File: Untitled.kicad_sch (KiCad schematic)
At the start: 49 parts, among them J1 USB_OTG, J2 Conn_02x03_Odd_Even, J3 Conn_02x08_Odd_Even, J4 CONN_01X14, J5 CONN_01X14, J6 USB_OTG, Q1 LM317AG-TN3-R, SW1 SW_Push, U1 ICE40LP8K-CM121, U4 iCE40-LP8K-CM81, U5 DSC6001CI2A-016.0000T, U6 AT25SF081-SSHD-B, U7 XC6206P332MR

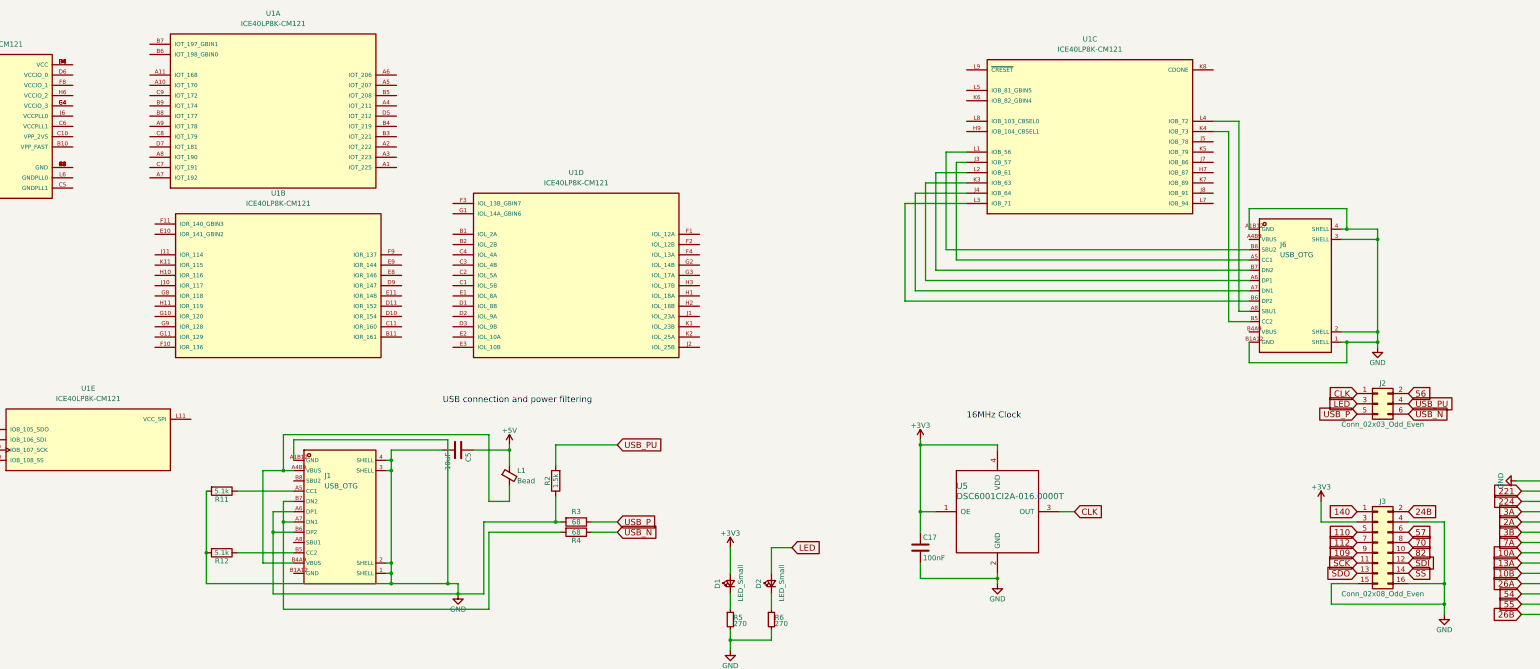
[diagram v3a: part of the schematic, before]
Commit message: Start connecting the board (reset + usb-c breakouts)
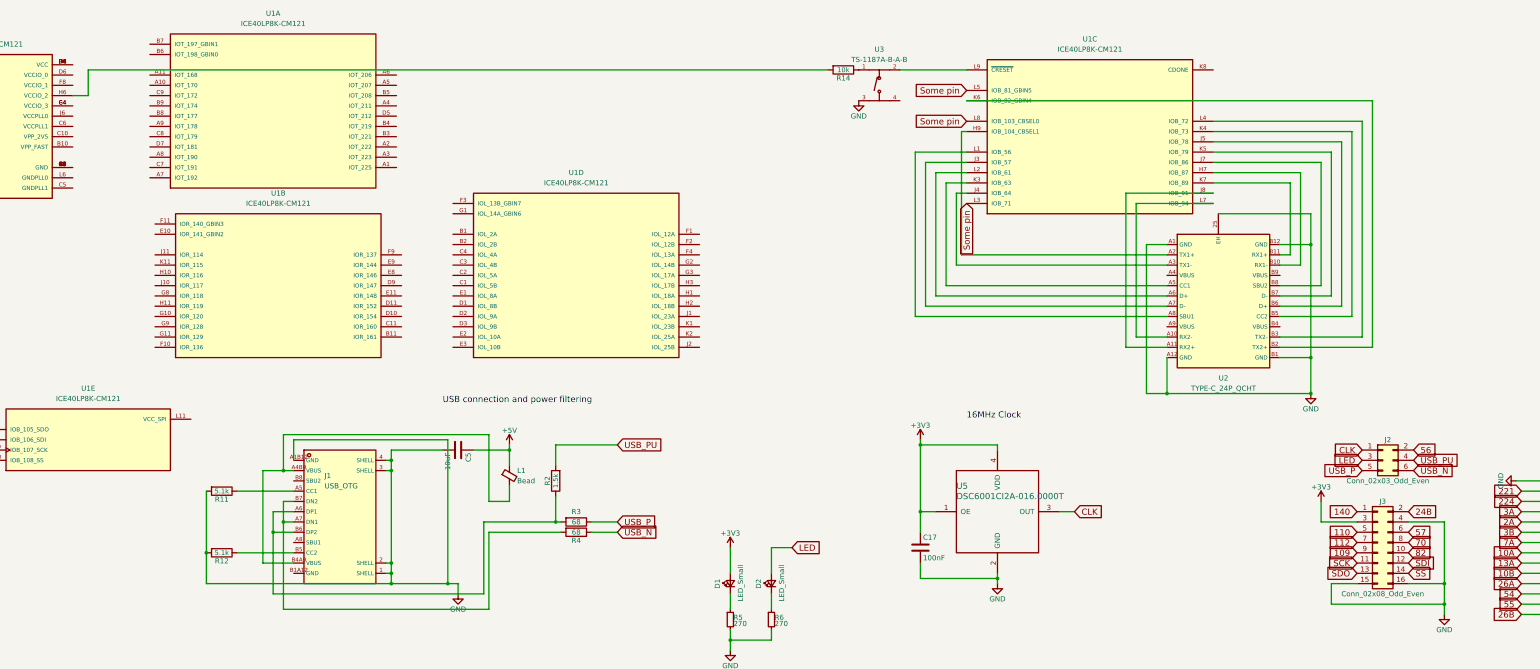
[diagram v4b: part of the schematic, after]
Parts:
- removed J6: USB_OTG, footprint:USB-C-SMD_G-SWITCH_GT-USB-7010ASV, symbol GT-USB-7010ASV:GT-USB-7010ASV
- added R14: 10k, Resistors_SMD:R_0402_NoSilk, symbol TinyFPGA-BX-rescue:R
- added U2: TYPE-C_24P_QCHT, footprint:TYPE-C-SMD_TYPE-C-24P-QCHT, symbol TYPE-C_24P_QCHT:TYPE-C_24P_QCHT
- added U3: TS-1187A-B-A-B, footprint:SW-SMD_4P-L5.1-W5.1-P3.70-LS6.5-TL-2, symbol TS-1187A-B-A-B:TS-1187A-B-A-B
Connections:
- net GND: now also U2.25 (EH), U2.A1 (GND), U2.A12 (GND), U2.B1 (GND), U2.B12 (GND), U3.3 (C); no longer J1.A6 (DP1), J1.B6 (DP2), R2.1, R3.2
- net at U1.H7 (IOB_87): now also U2.B10 (RX1-)
- net at U1.H9 (IOB_104_CBSEL1): now also U2.A2 (TX1+)
- net at U1.J3 (IOB_57): now also U2.A7 (D-)
- net at U1.J4 (IOB_64): now also U2.A3 (TX1-)
- net at U1.J5 (IOB_78): now also U2.B6 (D+)
- net at U1.J7 (IOB_86): now also U2.B8 (SBU2)
- net at U1.J8 (IOB_91): now also U2.A11 (RX2+)
- net at U1.K3 (IOB_63): now also U2.A5 (CC1)
- net at U1.K4 (IOB_73): now also U2.B5 (CC2)
- net at U1.K5 (IOB_79): now also U2.B7 (D-)
- net at U1.K6 (IOB_82_GBIN4): now also U2.B2 (TX2+)
- net at U1.K7 (IOB_89): now also U2.B11 (RX1+)
- net at U1.L1 (IOB_56): now also U2.A8 (SBU1)
- net at U1.L2 (IOB_61): now also U2.A6 (D+)
- net Some pin: now reaches U1.L3 (IOB_71)
- net Some pin: now also U1.L5 (IOB_81_GBIN5), U1.L8 (IOB_103_CBSEL0)
- net at U1.L4 (IOB_72): now also U2.B3 (TX2-)
- net at U1.L7 (IOB_94): now also U2.A10 (RX2-)
- net at U1.L9 (~{CRESET}): now also U3.2 (B)
- net at U1.H6 (VCCIO_2): now also R14.2
- new net: R14.1, U3.1 (A)
- new net: J1.A6 (DP1), J1.B6 (DP2), R2.1, R3.2
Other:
- moved on the sheet: J2

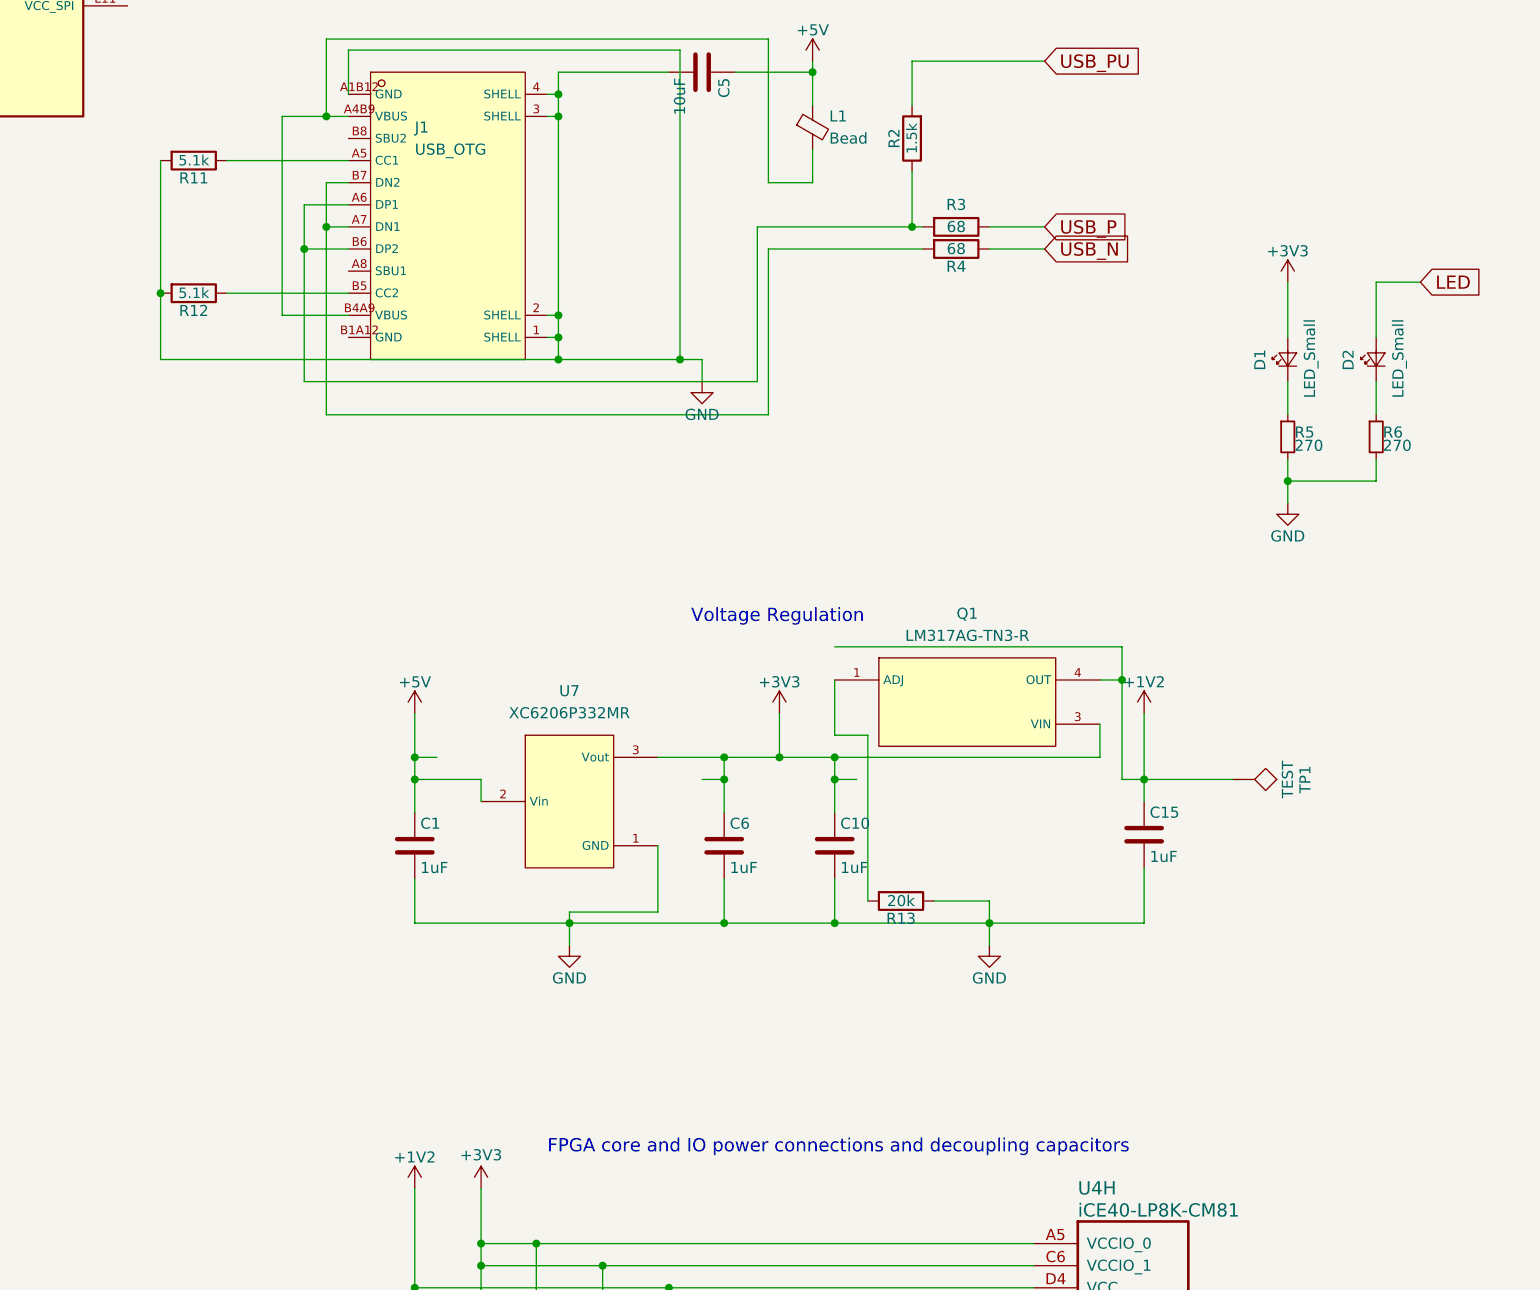
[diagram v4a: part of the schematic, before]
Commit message: Replace 16p usb-c with 24p usb-c
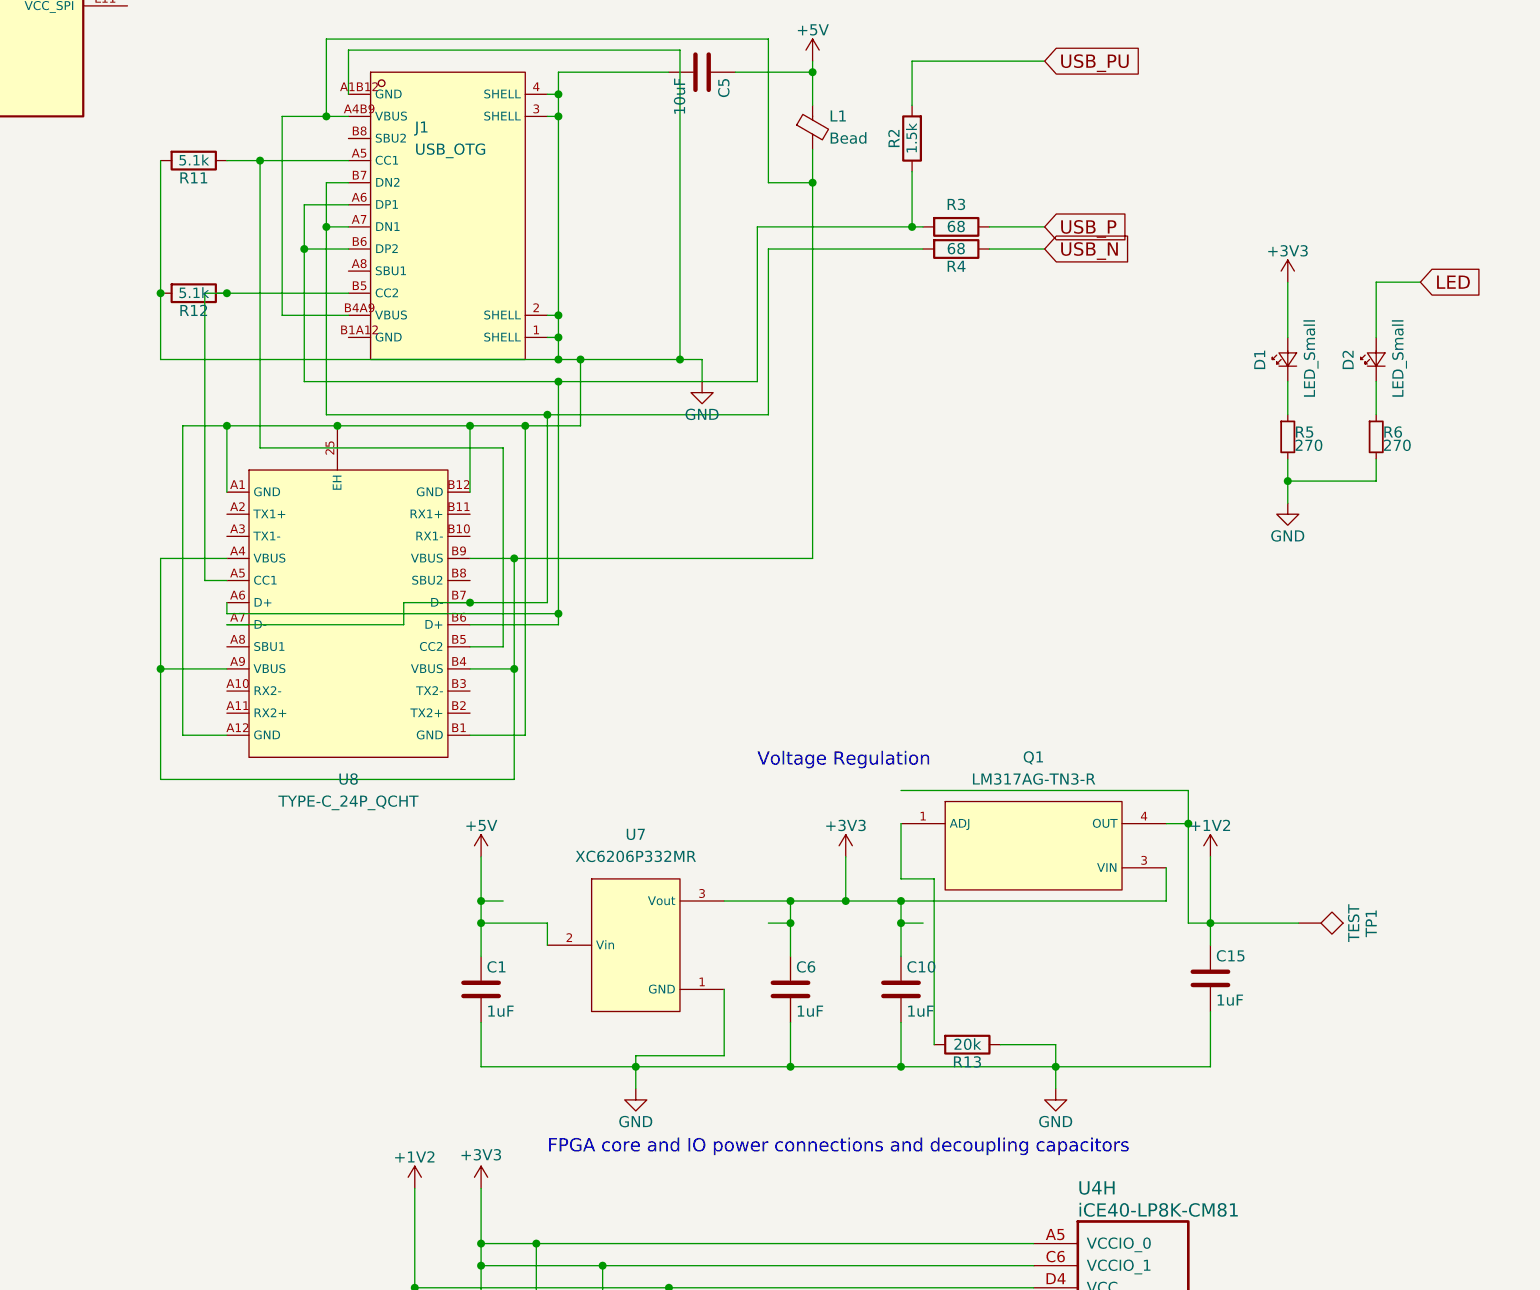
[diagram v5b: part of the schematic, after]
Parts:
- added U8: TYPE-C_24P_QCHT, footprint:TYPE-C-SMD_TYPE-C-24P-QCHT, symbol TYPE-C_24P_QCHT:TYPE-C_24P_QCHT
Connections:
- net GND: now also U8.25 (EH), U8.A1 (GND), U8.A12 (GND), U8.B1 (GND), U8.B12 (GND)
- net at J1.A5 (CC1), R11.1: now also U8.B5 (CC2)
- net at J1.A7 (DN1), J1.B7 (DN2), R4.2: now also U8.A7 (D-), U8.B7 (D-)
- net at J1.B5 (CC2), R12.1: now also U8.A5 (CC1)
- net at J1.A4B9 (VBUS), J1.B4A9 (VBUS), L1.2: now also U8.A4 (VBUS), U8.A9 (VBUS), U8.B4 (VBUS), U8.B9 (VBUS)
- net at J1.A6 (DP1), J1.B6 (DP2), R2.1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: now also U8.A6 (D+), U8.B6 (D+)
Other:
- moved on the sheet: C1, C10, C15, C6, Q1, R13, TP1, U7

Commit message: Finish wiring PIO (no DPIO yet) and add Mems and Flash
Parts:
- removed J1: USB_OTG, footprint:USB-C-SMD_G-SWITCH_GT-USB-7010ASV, symbol GT-USB-7010ASV:GT-USB-7010ASV
- added U10: W25Q128JVSIQTR, footprint:SOIC-8_L5.3-W5.3-P1.27-LS8.0-BL, symbol W25Q128JVSIQTR:W25Q128JVSIQTR
- added U11, U9: TYPE-C_24P_QCHT, footprint:TYPE-C-SMD_TYPE-C-24P-QCHT, symbol TYPE-C_24P_QCHT:TYPE-C_24P_QCHT
- added U12: DSC1001DI5-024_0000, footprint:OSC-SMD_4P-L2.5-W2.0-BL-A, symbol DSC1001DI5-024_0000:DSC1001DI5-024_0000
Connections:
- net +1V2: now also Q1.1 (ADJ), R13.2
- net +3V3: now also U1.L11 (VCC_SPI)
- net GND: now also U1.E5 (GND), U1.E6 (GND), U1.E7 (GND), U1.F5 (GND), U1.F6 (GND), U1.F7 (GND), U1.G5 (GND), U1.G6 (GND), U1.G7 (GND), U1.H5 (GND), U11.25 (EH), U11.A1 (GND), U11.A12 (GND), U11.B1 (GND), U11.B12 (GND), U9.25 (EH), U9.A1 (GND), U9.A12 (GND), U9.B1 (GND), U9.B12 (GND)
- net Some pin: now also U1.A1 (IOT_225), U1.A10 (IOT_170), U1.A11 (IOT_168), U1.A6 (IOT_206), U1.A7 (IOT_192), U1.B7 (IOT_197_GBIN1), U1.C9 (IOT_172), U1.F11 (IOR_140_GBIN3), U1.F9 (IOR_137), U1.H10 (IOR_116), U1.J11 (IOR_114), U1.J9 (IOB_106_SDI), U1.K10 (IOB_108_SS), U1.K11 (IOR_115), U1.K9 (IOB_105_SDO), U1.L10 (IOB_107_SCK)
- net at U1.B11 (IOR_161): now also U9.B11 (RX1+)
- net at U1.C11 (IOR_160): now also U9.B10 (RX1-)
- net at U1.D10 (IOR_154): now also U9.B8 (SBU2)
- net at U1.D11 (IOR_152): now also U9.B7 (D-)
- net at U1.D9 (IOR_147): now also U9.B5 (CC2)
- net at U1.E10 (IOR_141_GBIN2): now also U9.A11 (RX2+)
- net at U1.E11 (IOR_148): now also U9.B6 (D+)
- net at U1.E8 (IOR_146): now also U9.B3 (TX2-)
- net at U1.E9 (IOR_144): now also U9.B2 (TX2+)
- net at U1.F10 (IOR_136): now also U9.A2 (TX1+)
- net at U1.G10 (IOR_120): now also U9.A6 (D+)
- net at U1.G11 (IOR_129): now also U9.A3 (TX1-)
- net at U1.G8 (IOR_118): now also U9.A8 (SBU1)
- net at U1.G9 (IOR_128): now also U9.A5 (CC1)
- net at U1.H11 (IOR_119): now also U9.A7 (D-)
- net at U1.J10 (IOR_117): now also U9.A10 (RX2-)
- net USB_3_RX_N: now reaches U8.A10 (RX2-)
- net USB_3_RX_N: now also U8.B10 (RX1-)
- net USB_3_RX_P: now reaches U8.A11 (RX2+)
- net USB_3_RX_P: now also U8.B11 (RX1+)
- net USB_3_TX_P: now reaches U8.A2 (TX1+)
- net USB_3_TX_P: now also U8.B2 (TX2+)
- net USB_3_TX_N: now reaches U8.A3 (TX1-)
- net USB_3_TX_N: now also U8.B3 (TX2-)
- net at U1.A2 (IOT_222): now also U11.B10 (RX1-)
- net at U1.A3 (IOT_223): now also U11.B11 (RX1+)
- net at U1.A4 (IOT_211): now also U11.B5 (CC2)
- net at U1.A5 (IOT_207): now also U11.B2 (TX2+)
- net at U1.A8 (IOT_190): now also U11.A3 (TX1-)
- net at U1.A9 (IOT_178): now also U11.A7 (D-)
- net at U1.B3 (IOT_221): now also U11.B8 (SBU2)
- net at U1.B4 (IOT_219): now also U11.B7 (D-)
- net at U1.B5 (IOT_208): now also U11.B3 (TX2-)
- net at U1.B6 (IOT_198_GBIN0): now also U11.A11 (RX2+)
- net at U1.B8 (IOT_177): now also U11.A8 (SBU1)
- net at U1.B9 (IOT_174): now also U11.A10 (RX2-)
- net at U1.C7 (IOT_191): now also U11.A2 (TX1+)
- net at U1.C8 (IOT_179): now also U11.A6 (D+)
- net at U1.D5 (IOT_212): now also U11.B6 (D+)
- net at U1.D7 (IOT_181): now also U11.A5 (CC1)
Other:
- note added: "Flash"
- note added: "Mems"
- moved on the sheet: C11, C12, C13, C14, C16, C17, C2, C3, C4, C7, C8, C9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
